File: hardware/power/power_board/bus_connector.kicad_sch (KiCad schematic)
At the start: 6 parts, among them J601 504050-1291, J603 504050-1091

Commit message: Checkpointing layout work on power board.
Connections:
- net BATTERY_- is gone; now on net GND: J603.1, J603.11 (MP1), J603.12 (MP2), J603.2, J603.6, J603.9
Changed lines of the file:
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@@
   (junction (at 201.93 100.33) (diameter 0) (color 0 0 0 0)
   )
-  (junction (at 121.92 123.19) (diameter 0) (color 0 0 0 0)
+  (junction (at 121.92 120.65) (diameter 0) (color 0 0 0 0)
+  )
+  (junction (at 144.78 123.19) (diameter 0) (color 0 0 0 0)
   )
   (junction (at 201.93 95.25) (diameter 0) (color 0 0 0 0)
@@
     (effects (font (size 1.27 1.27)) (justify left top))
   )
-  (global_label "BATTERY_-" (shape input) (at 144.78 120.65 0) (fields_autoplaced)
-    (effects (font (size 1.27 1.27)) (justify left))
-    (property "Intersheetrefs" "${INTERSHEET_REFS}" (at 158.1066 120.65 0)
-      (effects (font (size 1.27 1.27)) (justify left))
-    )
-  )
-  (global_label "BATTERY_-" (shape input) (at 121.92 120.65 180) (fields_autoplaced)
-    (effects (font (size 1.27 1.27)) (justify right))
-    (property "Intersheetrefs" "${INTERSHEET_REFS}" (at 108.5934 120.65 0)
-      (effects (font (size 1.27 1.27)) (justify right))
-    )
-  )
   (global_label "THERMISTOR" (shape input) (at 121.92 135.89 180) (fields_autoplaced)
     (effects (font (size 1.27 1.27)) (justify right))
@@
     )
   )
-  (global_label "BATTERY_-" (shape input) (at 121.92 140.97 180) (fields_autoplaced)
-    (effects (font (size 1.27 1.27)) (justify right))
-    (property "Intersheetrefs" "${INTERSHEET_REFS}" (at 108.5934 140.97 0)
-      (effects (font (size 1.27 1.27)) (justify right))
-    )
-  )
   (global_label "POWER_SDA" (shape input) (at 115.57 59.69 180) (fields_autoplaced)
     (effects (font (size 1.27 1.27)) (justify right))
@@
     (effects (font (size 1.27 1.27)) (justify right))
     (property "Intersheetrefs" "${INTERSHEET_REFS}" (at 108.291 143.51 0)
-      (effects (font (size 1.27 1.27)) (justify right))
-    )
-  )
-  (global_label "BATTERY_-" (shape input) (at 121.92 133.35 180) (fields_autoplaced)
-    (effects (font (size 1.27 1.27)) (justify right))
-    (property "Intersheetrefs" "${INTERSHEET_REFS}" (at 108.5934 133.35 0)
       (effects (font (size 1.27 1.27)) (justify right))
     )
@@
     )
   )
+  (symbol (lib_id "power:GND") (at 121.92 133.35 270) (unit 1)
+    (in_bom yes) (on_board yes) (dnp no) (fields_autoplaced)
+    (property "Reference" "#PWR04" (at 115.57 133.35 0)
+      (effects (font (size 1.27 1.27)) hide)
+    )
+    (property "Value" "GND" (at 118.11 133.35 90)
+      (effects (font (size 1.27 1.27)) (justify right))
+    )
+    (property "Footprint" "" (at 121.92 133.35 0)
+      (effects (font (size 1.27 1.27)) hide)
+    )
+    (property "Datasheet" "" (at 121.92 133.35 0)
+      (effects (font (size 1.27 1.27)) hide)
+    )
+    (pin "1")
+    (instances
+      (project "power_board"
+        (path "/d7fbba2e-84c5-4e09-9d36-52dae726d12d/f5dda946-81da-4978-88f4-4ac2bc2b63d0"
+          (reference "#PWR04") (unit 1)
+        )
+      )
+    )
+  )
   (symbol (lib_id "power:GND") (at 115.57 62.23 270) (unit 1)
     (in_bom yes) (on_board yes) (dnp no) (fields_autoplaced)
@@
         (path "/d7fbba2e-84c5-4e09-9d36-52dae726d12d/f5dda946-81da-4978-88f4-4ac2bc2b63d0"
           (reference "#PWR0606") (unit 1)
+        )
+      )
+    )
+  )
+  (symbol (lib_id "power:GND") (at 121.92 140.97 270) (unit 1)
+    (in_bom yes) (on_board yes) (dnp no) (fields_autoplaced)
+    (property "Reference" "#PWR03" (at 115.57 140.97 0)
+      (effects (font (size 1.27 1.27)) hide)
+    )
+    (property "Value" "GND" (at 118.11 140.97 90)
+      (effects (font (size 1.27 1.27)) (justify right))
+    )
+    (property "Footprint" "" (at 121.92 140.97 0)
+      (effects (font (size 1.27 1.27)) hide)
+    )
+    (property "Datasheet" "" (at 121.92 140.97 0)
+      (effects (font (size 1.27 1.27)) hide)
+    )
+    (pin "1")
+    (instances
+      (project "power_board"
+        (path "/d7fbba2e-84c5-4e09-9d36-52dae726d12d/f5dda946-81da-4978-88f4-4ac2bc2b63d0"
+          (reference "#PWR03") (unit 1)
         )
       )
@@
     )
   )
+  (symbol (lib_id "power:GND") (at 144.78 123.19 0) (unit 1)
+    (in_bom yes) (on_board yes) (dnp no) (fields_autoplaced)
+    (property "Reference" "#PWR01" (at 144.78 129.54 0)
+      (effects (font (size 1.27 1.27)) hide)
+    )
+    (property "Value" "GND" (at 144.78 128.27 0)
+      (effects (font (size 1.27 1.27)))
+    )
+    (property "Footprint" "" (at 144.78 123.19 0)
+      (effects (font (size 1.27 1.27)) hide)
+    )
+    (property "Datasheet" "" (at 144.78 123.19 0)
+      (effects (font (size 1.27 1.27)) hide)
+    )
+    (pin "1")
+    (instances
+      (project "power_board"
+        (path "/d7fbba2e-84c5-4e09-9d36-52dae726d12d/f5dda946-81da-4978-88f4-4ac2bc2b63d0"
+          (reference "#PWR01") (unit 1)
+        )
+      )
+    )
+  )
   (symbol (lib_id "power:+5V") (at 115.57 64.77 90) (unit 1)
     (in_bom yes) (on_board yes) (dnp no) (fields_autoplaced)
@@
     )
   )
-  (symbol (lib_id "power:PWR_FLAG") (at 121.92 123.19 90) (unit 1)
-    (in_bom yes) (on_board yes) (dnp no) (fields_autoplaced)
-    (property "Reference" "#FLG0601" (at 120.015 123.19 0)
-      (effects (font (size 1.27 1.27)) hide)
-    )
-    (property "Value" "PWR_FLAG" (at 118.11 123.19 90)
-      (effects (font (size 1.27 1.27)) (justify left))
-    )
-    (property "Footprint" "" (at 121.92 123.19 0)
-      (effects (font (size 1.27 1.27)) hide)
-    )
-    (property "Datasheet" "~" (at 121.92 123.19 0)
-      (effects (font (size 1.27 1.27)) hide)
-    )
-    (pin "1")
-    (instances
-      (project "power_board"
-        (path "/d7fbba2e-84c5-4e09-9d36-52dae726d12d/f5dda946-81da-4978-88f4-4ac2bc2b63d0"
-          (reference "#FLG0601") (unit 1)
-        )
-      )
-    )
-  )
   (symbol (lib_id "power:PWR_FLAG") (at 121.92 128.27 90) (unit 1)
     (in_bom yes) (on_board yes) (dnp no) (fields_autoplaced)
@@
         (path "/d7fbba2e-84c5-4e09-9d36-52dae726d12d/f5dda946-81da-4978-88f4-4ac2bc2b63d0"
           (reference "#FLG0602") (unit 1)
+        )
+      )
+    )
+  )
+  (symbol (lib_id "power:PWR_FLAG") (at 121.92 120.65 0) (unit 1)
+    (in_bom yes) (on_board yes) (dnp no) (fields_autoplaced)
+    (property "Reference" "#FLG01" (at 121.92 118.745 0)
+      (effects (font (size 1.27 1.27)) hide)
+    )
+    (property "Value" "PWR_FLAG" (at 121.92 115.57 0)
+      (effects (font (size 1.27 1.27)))
+    )
+    (property "Footprint" "" (at 121.92 120.65 0)
+      (effects (font (size 1.27 1.27)) hide)
+    )
+    (property "Datasheet" "~" (at 121.92 120.65 0)
+      (effects (font (size 1.27 1.27)) hide)
+    )
+    (pin "1")
+    (instances
+      (project "power_board"
+        (path "/d7fbba2e-84c5-4e09-9d36-52dae726d12d/f5dda946-81da-4978-88f4-4ac2bc2b63d0"
+          (reference "#FLG01") (unit 1)
         )
       )
@@
         )
       )
+    )
+  )
+  (symbol (lib_id "power:GND") (at 121.92 120.65 270) (unit 1)
+    (in_bom yes) (on_board yes) (dnp no) (fields_autoplaced)
+    (property "Reference" "#PWR02" (at 115.57 120.65 0)
+      (effects (font (size 1.27 1.27)) hide)
+    )
+    (property "Value" "GND" (at 118.11 120.65 90)
+      (effects (font (size 1.27 1.27)) (justify right))
+    )
+    (property "Footprint" "" (at 121.92 120.65 0)
+      (effects (font (size 1.27 1.27)) hide)
+    )
+    (property "Datasheet" "" (at 121.92 120.65 0)
+      (effects (font (size 1.27 1.27)) hide)
+    )
+    (pin "1")
+    (instances
+      (project "power_board"
+        (path "/d7fbba2e-84c5-4e09-9d36-52dae726d12d/f5dda946-81da-4978-88f4-4ac2bc2b63d0"
+          (reference "#PWR02") (unit 1)
+        )
+      )

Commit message: Checkpointing work
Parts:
- J601: footprint 5040501291 -> (none)
- J603: footprint 504050-1091 -> (none)
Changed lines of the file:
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@@
       (effects (font (size 1.27 1.27)))
     )
-    (property "Footprint" "5040501291" (at 137.16 149.53 0)
+    (property "Footprint" "" (at 137.16 149.53 0)
       (effects (font (size 1.27 1.27)) (justify left top) hide)
     )
@@
       (effects (font (size 1.524 1.524)))
     )
-    (property "Footprint" "504050-1091" (at 140.97 215.57 0)
-      (effects (font (size 1.27 1.27)) (justify left top) hide)
-    )
+    (property "Footprint" "" (at 140.97 215.57 0)
+      (effects (font (size 1.27 1.27)) (justify left top) hide)
+    )

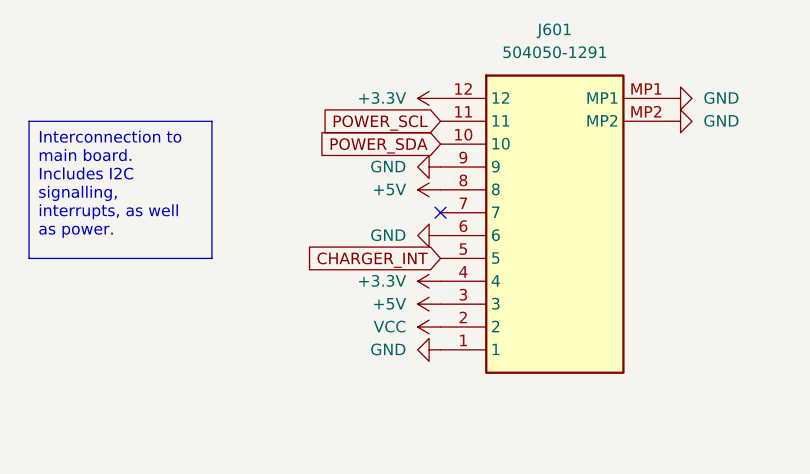
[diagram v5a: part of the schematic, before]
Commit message: Placed all parts on power board PCB
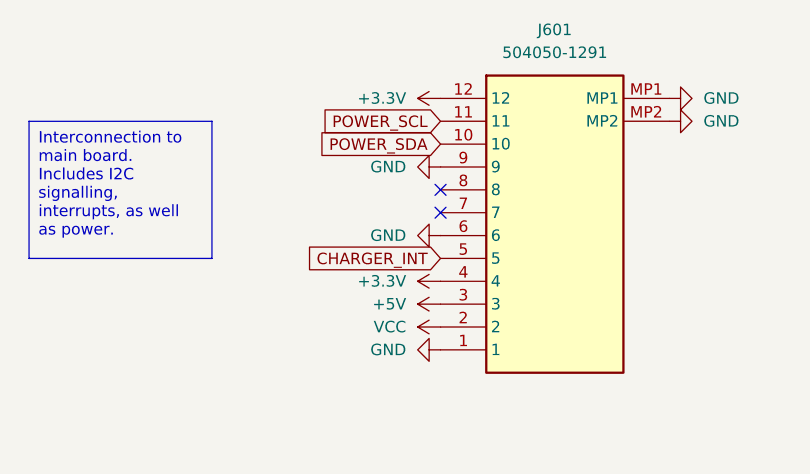
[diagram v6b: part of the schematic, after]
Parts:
- J601: footprint (none) -> footprints:5040501291
- J603: footprint (none) -> footprints:504050-1091
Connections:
- net +5V: no longer J601.8
- no-connect marks 3 -> 4
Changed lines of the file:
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@@
   )
   (no_connect (at 115.57 67.31))
+  (no_connect (at 115.57 64.77))
   (no_connect (at 121.92 138.43))
   (no_connect (at 121.92 130.81))
@@
       (effects (font (size 1.27 1.27)))
     )
-    (property "Footprint" "" (at 137.16 149.53 0)
+    (property "Footprint" "footprints:5040501291" (at 137.16 149.53 0)
       (effects (font (size 1.27 1.27)) (justify left top) hide)
     )
@@
     )
   )
-  (symbol (lib_id "power:+5V") (at 115.57 64.77 90) (unit 1)
-    (in_bom yes) (on_board yes) (dnp no) (fields_autoplaced)
-    (property "Reference" "#PWR0603" (at 119.38 64.77 0)
-      (effects (font (size 1.27 1.27)) hide)
-    )
-    (property "Value" "+5V" (at 111.76 64.77 90)
-      (effects (font (size 1.27 1.27)) (justify left))
-    )
-    (property "Footprint" "" (at 115.57 64.77 0)
-      (effects (font (size 1.27 1.27)) hide)
-    )
-    (property "Datasheet" "" (at 115.57 64.77 0)
-      (effects (font (size 1.27 1.27)) hide)
-    )
-    (pin "1")
-    (instances
-      (project "power_board"
-        (path "/d7fbba2e-84c5-4e09-9d36-52dae726d12d/f5dda946-81da-4978-88f4-4ac2bc2b63d0"
-          (reference "#PWR0603") (unit 1)
-        )
-      )
-    )
-  )
   (symbol (lib_id "mounting:Mounting_Hole_M3_ISO_7380") (at 201.93 90.17 0) (unit 1)
     (in_bom no) (on_board yes) (dnp no) (fields_autoplaced)
@@
       (effects (font (size 1.524 1.524)))
     )
-    (property "Footprint" "" (at 140.97 215.57 0)
-      (effects (font (size 1.27 1.27)) (justify left top) hide)
-    )
+    (property "Footprint" "footprints:504050-1091" (at 140.97 215.57 0)
+      (effects (font (size 1.27 1.27)) (justify left top) hide)
+    )
